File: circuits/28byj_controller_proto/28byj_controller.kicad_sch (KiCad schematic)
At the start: 13 parts, among them J1 INPUT, J2 5V, M1 28BYJ-48_Stepper, M2 28BYJ-48_Stepper, U1 74HC595, U2 ULN2803A

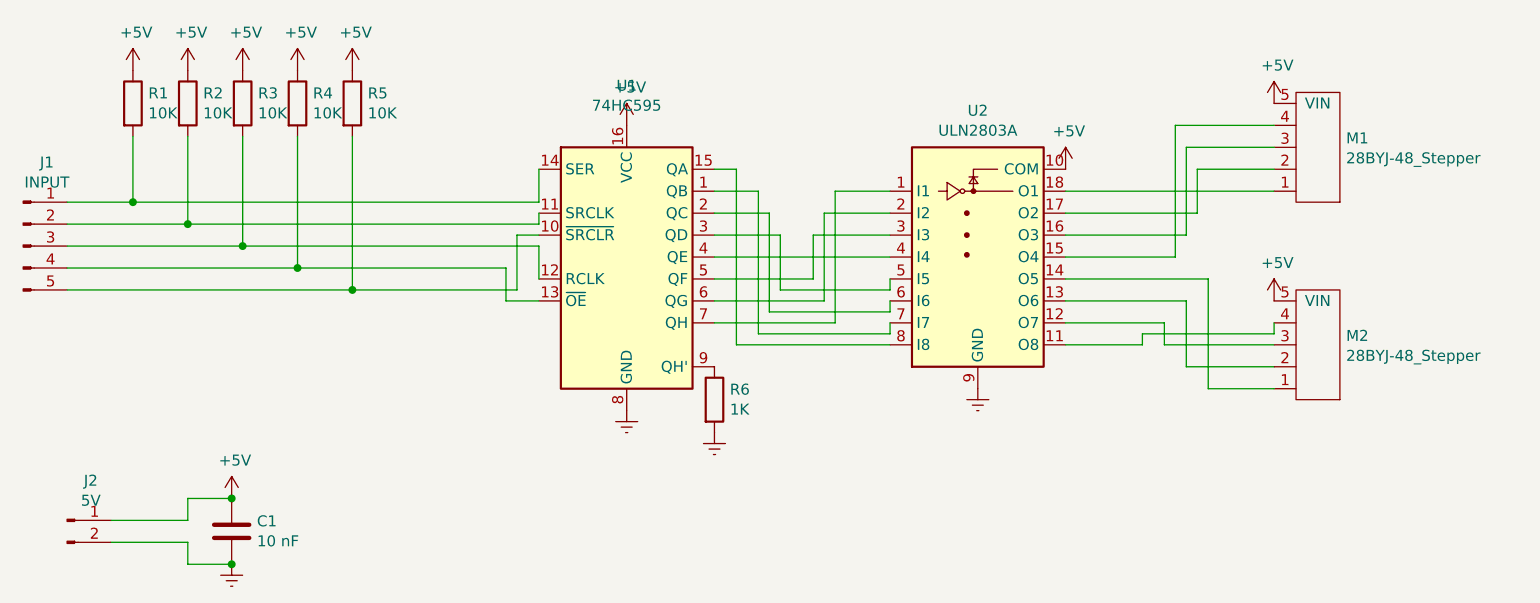
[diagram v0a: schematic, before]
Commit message: Code works and is tested on waveforms.
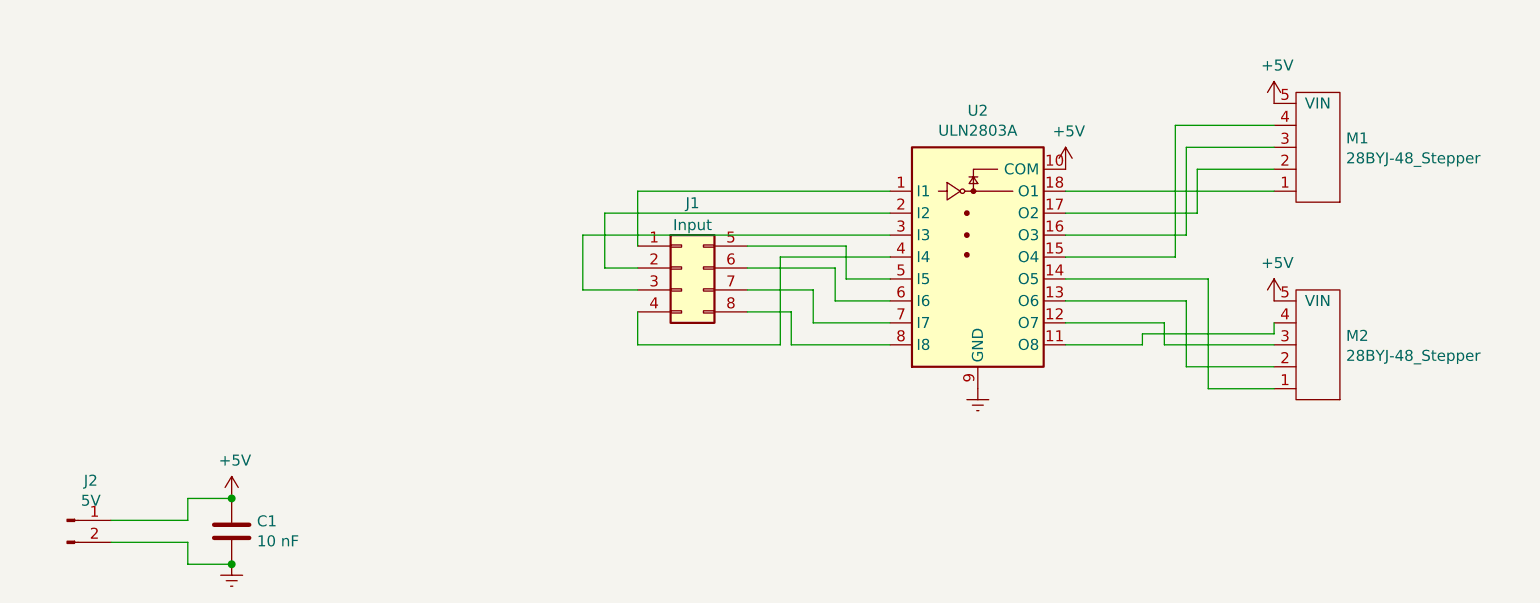
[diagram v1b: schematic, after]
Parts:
- removed J1: INPUT, Connector_PinSocket_2.54mm:PinSocket_1x05_P2.54mm_Vertical, symbol Connector:Conn_01x05_Male
- removed R1, R2, R3, R4, R5: 10K, Resistor_SMD:R_0805_2012Metric_Pad1.20x1.40mm_HandSolder, symbol Device:R
- removed R6: 1K, Resistor_SMD:R_0805_2012Metric_Pad1.20x1.40mm_HandSolder, symbol Device:R
- removed U1: 74HC595, Package_SO:SO-16_3.9x9.9mm_P1.27mm, symbol 74xx:74HC595
- added J1: Input, Connector_PinHeader_2.54mm:PinHeader_2x04_P2.54mm_Vertical, symbol Connector_Generic:Conn_02x04_Top_Bottom
- J2: footprint Connector_PinSocket_2.54mm:PinSocket_1x02_P2.54mm_Vertical -> Connector_JST:JST_XH_B2B-XH-AM_1x02_P2.50mm_Vertical
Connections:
- net at U2.7 (I7): now also J1.7 (Pin_7)
- net at U2.8 (I8): now also J1.8 (Pin_8)
- net at U2.6 (I6): now also J1.6 (Pin_6)
- net at U2.5 (I5): now also J1.5 (Pin_5)
- net at U2.4 (I4): now also J1.4 (Pin_4)
- net at U2.3 (I3): now also J1.3 (Pin_3)
- net at U2.2 (I2): now also J1.2 (Pin_2)
- net at U2.1 (I1): now also J1.1 (Pin_1)

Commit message: Modified some circuits.
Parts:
- added R1, R2, R3, R4, R5, R6, R7, R8: 10 K, Resistor_SMD:R_0805_2012Metric_Pad1.20x1.40mm_HandSolder, symbol Device:R
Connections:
- net +5V: now also R1.1, R2.2, R3.1, R4.2, R5.1, R6.2, R7.1, R8.2
- net at J1.1 (Pin_1), U2.1 (I1): now also R1.2
- net at J1.2 (Pin_2), U2.2 (I2): now also R5.2
- net at J1.3 (Pin_3), U2.3 (I3): now also R7.2
- net at J1.4 (Pin_4), U2.4 (I4): now also R2.1
- net at J1.5 (Pin_5), U2.5 (I5): now also R8.1
- net at J1.6 (Pin_6), U2.6 (I6): now also R6.1
- net at J1.7 (Pin_7), U2.7 (I7): now also R3.2
- net at J1.8 (Pin_8), U2.8 (I8): now also R4.1
